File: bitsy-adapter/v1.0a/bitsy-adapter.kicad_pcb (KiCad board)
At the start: 2 copper layers, 49.5 x 36.8 mm, 17 parts, among them J1 PMOD1A, J2 PMOD1A, J3 PMOD1A, J4 5V AUX, J5 5V AUX, J6 5V AUX

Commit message: Finish bitsy-adapter v1.0a
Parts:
- removed the J5 at (160.0, 102.9)
- added J6: IO3, pkl_pin_headers:Pin_Header_Straight_Round_1x01, F.Cu at (147.3, 119.4)
- added J7: IO2, pkl_pin_headers:Pin_Header_Straight_Round_1x01, F.Cu at (149.9, 119.4)
- added LOGO1: 1BitSquared, pkl_logos:null_Logo_SilkS_4mm, B.Cu at (139.7, 130.2)
- moved A1 5.08 mm to (133.3, 114.3)
- moved R1 0.63 mm to (123.4, 103.5)
- moved R2 0.63 mm to (128.5, 103.5)
- moved R3 0.63 mm to (146.3, 103.5)
- moved R4 0.63 mm to (151.4, 103.5)
- moved R5 0.63 mm to (156.8, 109.5)
- moved R6 0.63 mm to (156.8, 114.6)
- renumbered J6 to J5
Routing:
- net GND: track 92.8 -> 101.0 mm
- net +5V: track 79.3 -> 85.0 mm
- net +3V3: track 63.2 -> 68.2 mm
- net /P2_10: track 31.1 -> 35.7 mm, vias 0 -> 1
- net /P2_8: track 18.8 -> 23.5 mm, vias 0 -> 1
- net /P2_4: track 28.3 -> 32.8 mm, vias 0 -> 1
- net /P2_2: track 16.0 -> 20.6 mm, vias 0 -> 1
- net /P2_7: track 13.3 -> 17.7 mm, vias 0 -> 1
- net /P2_9: track 25.5 -> 30.0 mm, vias 0 -> 1
- net /P2_1: track 10.5 -> 14.9 mm, vias 0 -> 1
- net /P2_3: track 22.7 -> 27.2 mm, vias 0 -> 1
- net /P1A9: track 24.1 -> 19.7 mm
- net /P1A7: track 22.0 -> 18.4 mm
- net /P1B9: track 6.07 -> 2.57 mm, vias 1 -> 0
- net /P1A8: track 22.5 -> 19.3 mm
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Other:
- board text added: ""5V" is connected to VIN on the Bitsy, which is in turn jumpered to VUSB"
- board text added: "1"
- board text added: "12"
- board text added: "3V3"
- board text added: "5V"
- board text added: "6"
- board text added: "7"
- board text added: "CC BY-SA 4.0"
- board text added: "GND"
- board text added: "IO2"
- board text added: "IO3"
- board text added: "P1A1"
- board text added: "P1A10"
- board text added: "P1A2"
- board text added: "P1A3"
- board text added: "P1A4"
- board text added: "P1A7"
- board text added: "P1A8"
- board text added: "P1A9"
- board text added: "P1B1"
- board text added: "P1B10"
- board text added: "P1B2"
- board text added: "P1B3"
- board text added: "P1B4"
- board text added: "P1B7"
- board text added: "P1B8"
- board text added: "P1B9"
- board text added: "P2_1"
- board text added: "P2_10"
- board text added: "P2_2"
- board text added: "P2_3"
- board text added: "P2_4"
- board text added: "P2_7"
- board text added: "P2_8"
- board text added: "P2_9"
- board text added: "PMOD1A"
- board text added: "PMOD1B"
- board text added: "PMOD2"
- board text added: "USB GOES HERE"
- board text added: "VIN"
- board text added: "iCEBreaker Bitsy PMOD Adapter"
- board text added: "iCEBreaker Bitsy PMOD Adapter v1.0a"
- board text added: "iCEBreaker Bitsy v1.x"
- board text added: "v1.0a"
- board text added: "© 2020 NULL"
- board text added: "© 2020 NULL CC BY-SA 4.0"
- board text removed: "iCEBreaker Bitsy"

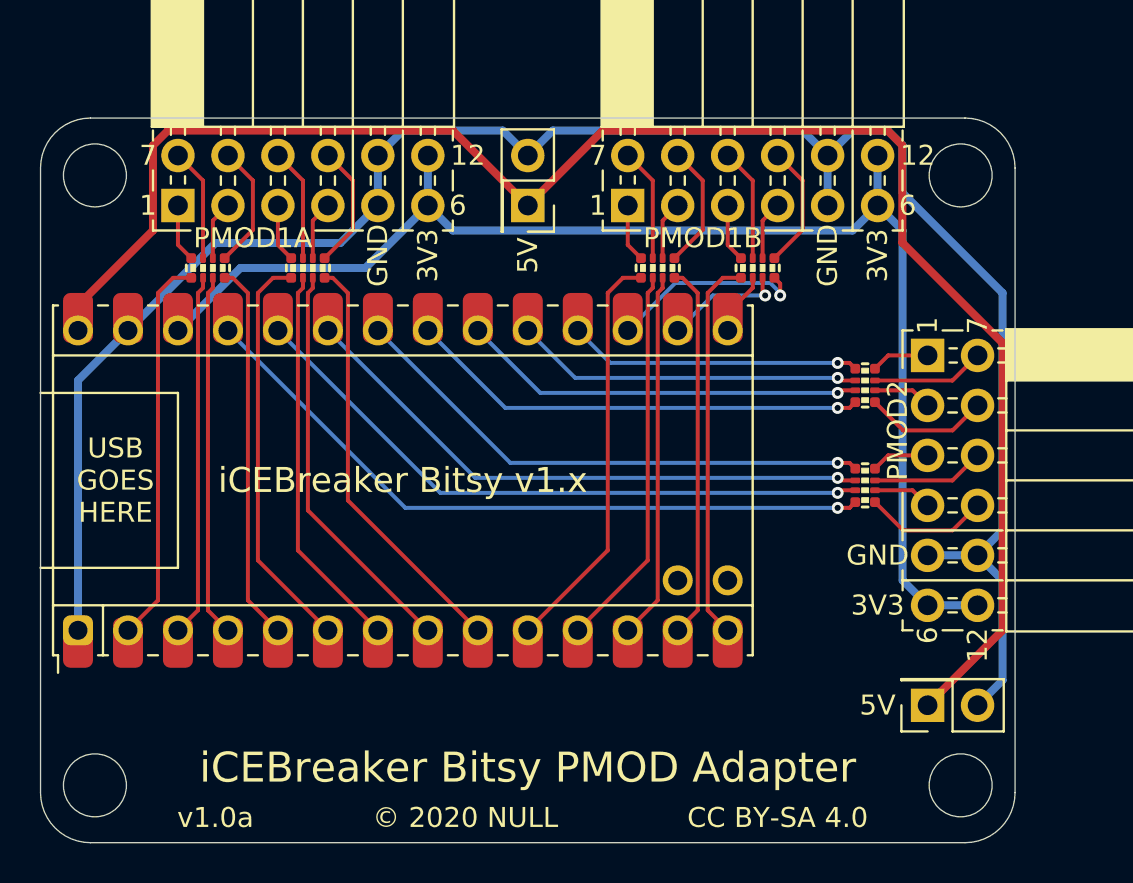
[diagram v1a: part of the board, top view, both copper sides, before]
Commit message: Change bitsy adapter pinout
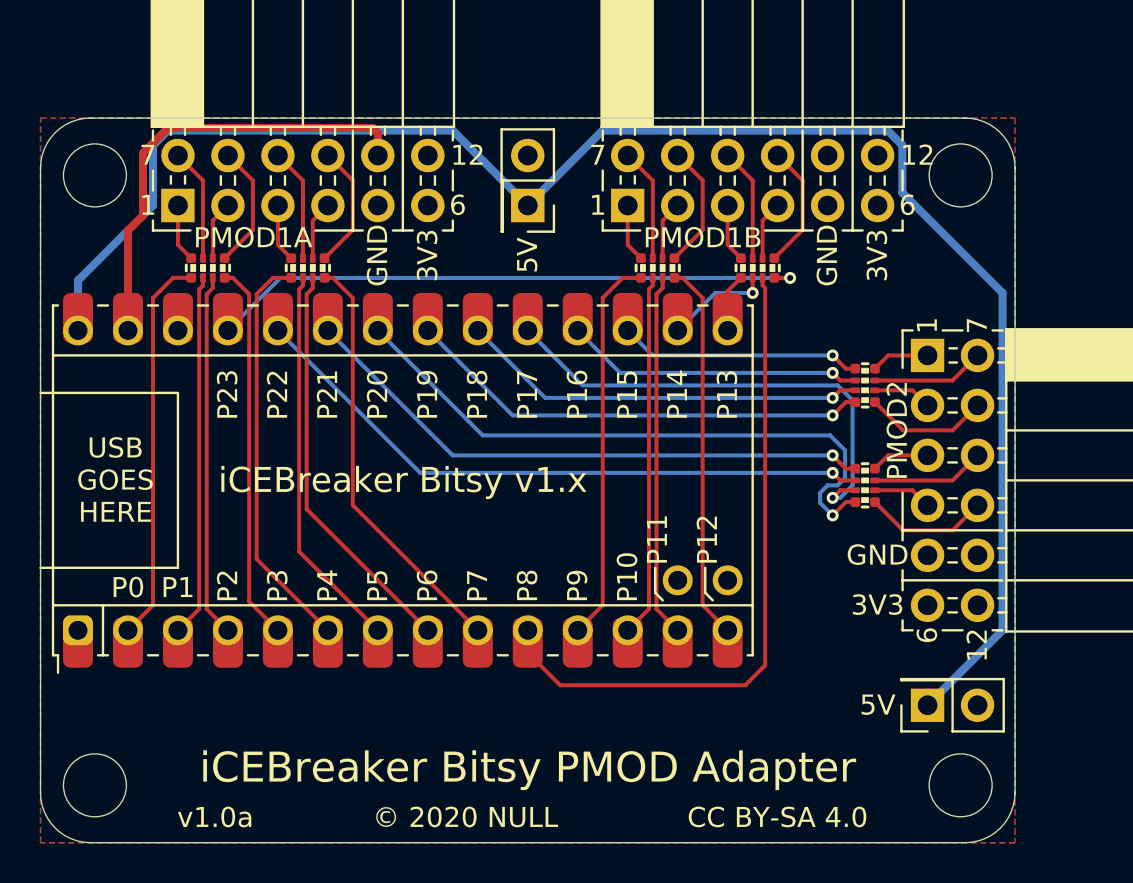
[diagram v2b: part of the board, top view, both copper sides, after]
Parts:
- J2: value PMOD1A -> PMOD1B
- J3: value PMOD1A -> PMOD2
- LOGO1: footprint pkl_logos:null_Logo_SilkS_4mm -> pkl_logos:1b2_Logo_SilkS_4mm
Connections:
- A1 pad 10: /P1B1 -> /P8
- A1 pad 11: /P1B7 -> /P9
- A1 pad 12: /P1B2 -> /P10
- A1 pad 13: /P1B8 -> /P11
- A1 pad 14: /P1B3 -> /P12
- A1 pad 15: /P1B9 -> /P13
- A1 pad 16: /P1B4 -> /P14
- A1 pad 17: /P1B10 -> /P15
- A1 pad 18: /P2_1 -> /P16
- A1 pad 19: /P2_7 -> /P17
- A1 pad 2: /P1A1 -> /P0
- A1 pad 20: /P2_2 -> /P18
- A1 pad 21: /P2_8 -> /P19
- A1 pad 22: /P2_3 -> /P20
- A1 pad 23: /P2_9 -> /P21
- A1 pad 24: /P2_4 -> /P22
- A1 pad 25: /P2_10 -> /P23
- A1 pad 3: /P1A7 -> /P1
- A1 pad 4: /P1A2 -> /P2
- A1 pad 5: /P1A8 -> /P3
- A1 pad 6: /P1A3 -> /P4
- A1 pad 7: /P1A9 -> /P5
- A1 pad 8: /P1A4 -> /P6
- A1 pad 9: /P1A10 -> /P7
- J1 pad 1: Net-(J1-Pad1) -> /P1A1
- J1 pad 10: Net-(J1-Pad10) -> /P1A10
- J1 pad 2: Net-(J1-Pad2) -> /P1A2
- J1 pad 3: Net-(J1-Pad3) -> /P1A3
- J1 pad 4: Net-(J1-Pad4) -> /P1A4
- J1 pad 7: Net-(J1-Pad7) -> /P1A7
- J1 pad 8: Net-(J1-Pad8) -> /P1A8
- J1 pad 9: Net-(J1-Pad9) -> /P1A9
- J2 pad 1: Net-(J2-Pad1) -> /P1B1
- J2 pad 10: Net-(J2-Pad10) -> /P1B10
- J2 pad 2: Net-(J2-Pad2) -> /P1B2
- J2 pad 3: Net-(J2-Pad3) -> /P1B3
- J2 pad 4: Net-(J2-Pad4) -> /P1B4
- J2 pad 7: Net-(J2-Pad7) -> /P1B7
- J2 pad 8: Net-(J2-Pad8) -> /P1B8
- J2 pad 9: Net-(J2-Pad9) -> /P1B9
- J3 pad 1: Net-(J3-Pad1) -> /P2_1
- J3 pad 10: Net-(J3-Pad10) -> /P2_10
- J3 pad 2: Net-(J3-Pad2) -> /P2_2
- J3 pad 3: Net-(J3-Pad3) -> /P2_3
- J3 pad 4: Net-(J3-Pad4) -> /P2_4
- J3 pad 7: Net-(J3-Pad7) -> /P2_7
- J3 pad 8: Net-(J3-Pad8) -> /P2_8
- J3 pad 9: Net-(J3-Pad9) -> /P2_9
- R1 pad 1: /P1A1 -> /P0
- R1 pad 2: Net-(J1-Pad1) -> /P1A1
- R1 pad 3: /P1A7 -> /P1
- R1 pad 4: Net-(J1-Pad7) -> /P1A7
- R1 pad 5: /P1A2 -> /P2
- R1 pad 6: Net-(J1-Pad2) -> /P1A2
- R1 pad 7: /P1A8 -> /P3
- R1 pad 8: Net-(J1-Pad8) -> /P1A8
- R2 pad 1: /P1A3 -> /P4
- R2 pad 2: Net-(J1-Pad3) -> /P1A3
- R2 pad 3: /P1A9 -> /P5
- R2 pad 4: Net-(J1-Pad9) -> /P1A9
- R2 pad 5: /P1A4 -> /P6
- R2 pad 6: Net-(J1-Pad4) -> /P1A4
- R2 pad 7: /P1A10 -> /P7
- R2 pad 8: Net-(J1-Pad10) -> /P1A10
- R3 pad 1: /P1B1 -> /P9
- R3 pad 2: Net-(J2-Pad1) -> /P1B1
- R3 pad 3: /P1B7 -> /P10
- R3 pad 4: Net-(J2-Pad7) -> /P1B7
- R3 pad 5: /P1B2 -> /P11
- R3 pad 6: Net-(J2-Pad2) -> /P1B2
- R3 pad 7: /P1B8 -> /P12
- R3 pad 8: Net-(J2-Pad8) -> /P1B8
- R4 pad 1: /P1B3 -> /P13
- R4 pad 2: Net-(J2-Pad3) -> /P1B3
- R4 pad 3: /P1B9 -> /P14
- R4 pad 4: Net-(J2-Pad9) -> /P1B9
- R4 pad 5: /P1B4 -> /P8
- R4 pad 6: Net-(J2-Pad4) -> /P1B4
- R4 pad 7: /P1B10 -> /P23
- R4 pad 8: Net-(J2-Pad10) -> /P1B10
- R5 pad 1: /P2_1 -> /P15
- R5 pad 2: Net-(J3-Pad1) -> /P2_1
- R5 pad 3: /P2_7 -> /P16
- R5 pad 4: Net-(J3-Pad7) -> /P2_7
- R5 pad 5: /P2_2 -> /P18
- R5 pad 6: Net-(J3-Pad2) -> /P2_2
- R5 pad 7: /P2_8 -> /P19
- R5 pad 8: Net-(J3-Pad8) -> /P2_8
- R6 pad 1: /P2_3 -> /P21
- R6 pad 2: Net-(J3-Pad3) -> /P2_3
- R6 pad 3: /P2_9 -> /P22
- R6 pad 4: Net-(J3-Pad9) -> /P2_9
- R6 pad 5: /P2_4 -> /P17
- R6 pad 6: Net-(J3-Pad4) -> /P2_4
- R6 pad 7: /P2_10 -> /P20
- R6 pad 8: Net-(J3-Pad10) -> /P2_10
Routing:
- net GND: track 101.0 -> 22.4 mm
- net +3V3: track 68.2 -> 0.00 mm
- net /P8: track 0.00 -> 33.4 mm
- net /P22: track 0.00 -> 32.5 mm, vias 0 -> 1
- net /P20: track 0.00 -> 32.1 mm, vias 0 -> 1
- net /P23: track 0.00 -> 30.5 mm, vias 0 -> 1
- net /P2_4: track 32.8 -> 2.99 mm, vias 1 -> 0
- net /P21: track 0.00 -> 29.7 mm, vias 0 -> 1
- net /P2_10: track 35.7 -> 6.34 mm, vias 1 -> 0
- net /P17: track 0.00 -> 24.9 mm, vias 0 -> 1
- net /P2_9: track 30.0 -> 5.74 mm, vias 1 -> 0
- net /P2_3: track 27.2 -> 2.95 mm, vias 1 -> 0
- net /P19: track 0.00 -> 23.8 mm, vias 0 -> 1
- net /P7: track 0.00 -> 21.4 mm
- net /P18: track 0.00 -> 20.8 mm, vias 0 -> 1
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- added copper zone on B.Cu, net +3V3
- added copper zone on F.Cu, net GND
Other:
- board text added: "P0"
- board text added: "P1"
- board text added: "P10"
- board text added: "P11"
- board text added: "P12"
- board text added: "P13"
- board text added: "P14"
- board text added: "P15"
- board text added: "P16"
- board text added: "P17"
- board text added: "P18"
- board text added: "P19"
- board text added: "P2"
- board text added: "P20"
- board text added: "P21"
- board text added: "P22"
- board text added: "P23"
- board text added: "P3"
- board text added: "P4"
- board text added: "P5"
- board text added: "P6"
- board text added: "P7"
- board text added: "P8"
- board text added: "P9"

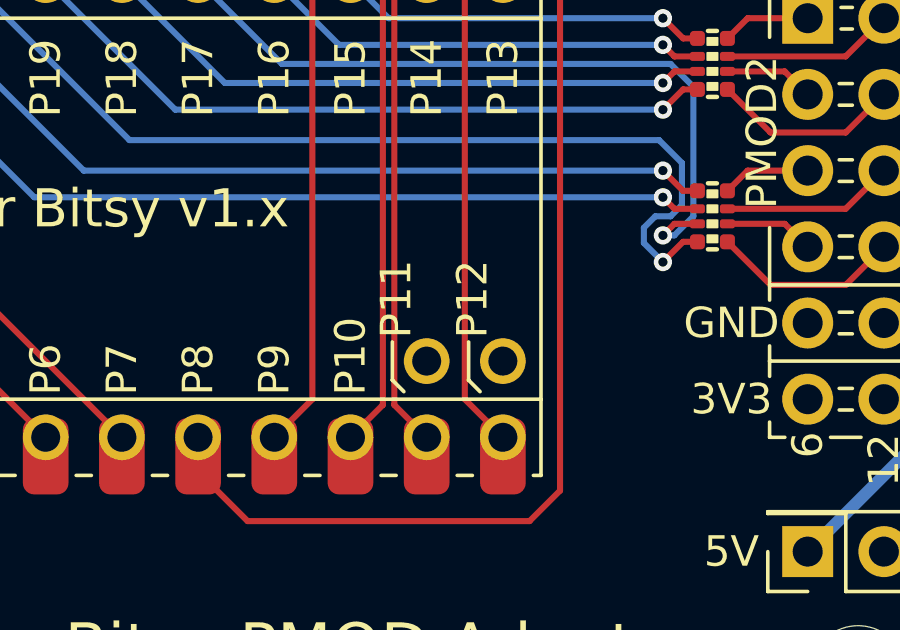
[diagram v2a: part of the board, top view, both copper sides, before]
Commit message: Bitsy Adapter: Remove unused IO2 & IO3 pins
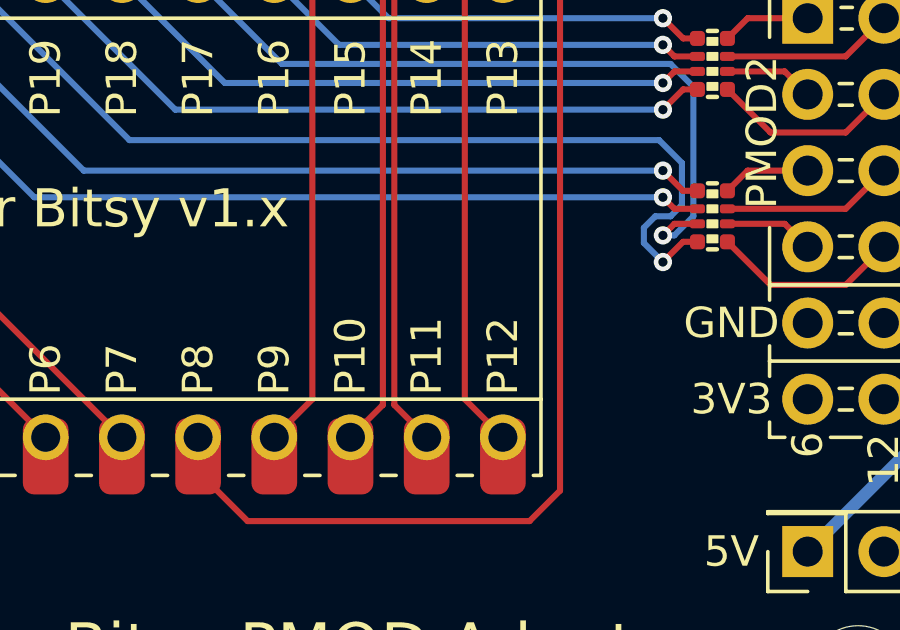
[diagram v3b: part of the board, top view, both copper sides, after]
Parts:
- removed J6: IO3, pkl_pin_headers:Pin_Header_Straight_Round_1x01
- removed J7: IO2, pkl_pin_headers:Pin_Header_Straight_Round_1x01
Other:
- board text added: "5V is connected to VIN on the Bitsy, which is in turn jumpered to VUSB"
- board text removed: ""5V" is connected to VIN on the Bitsy, which is in turn jumpered to VUSB"
- board text removed: "IO2"
- board text removed: "IO3"

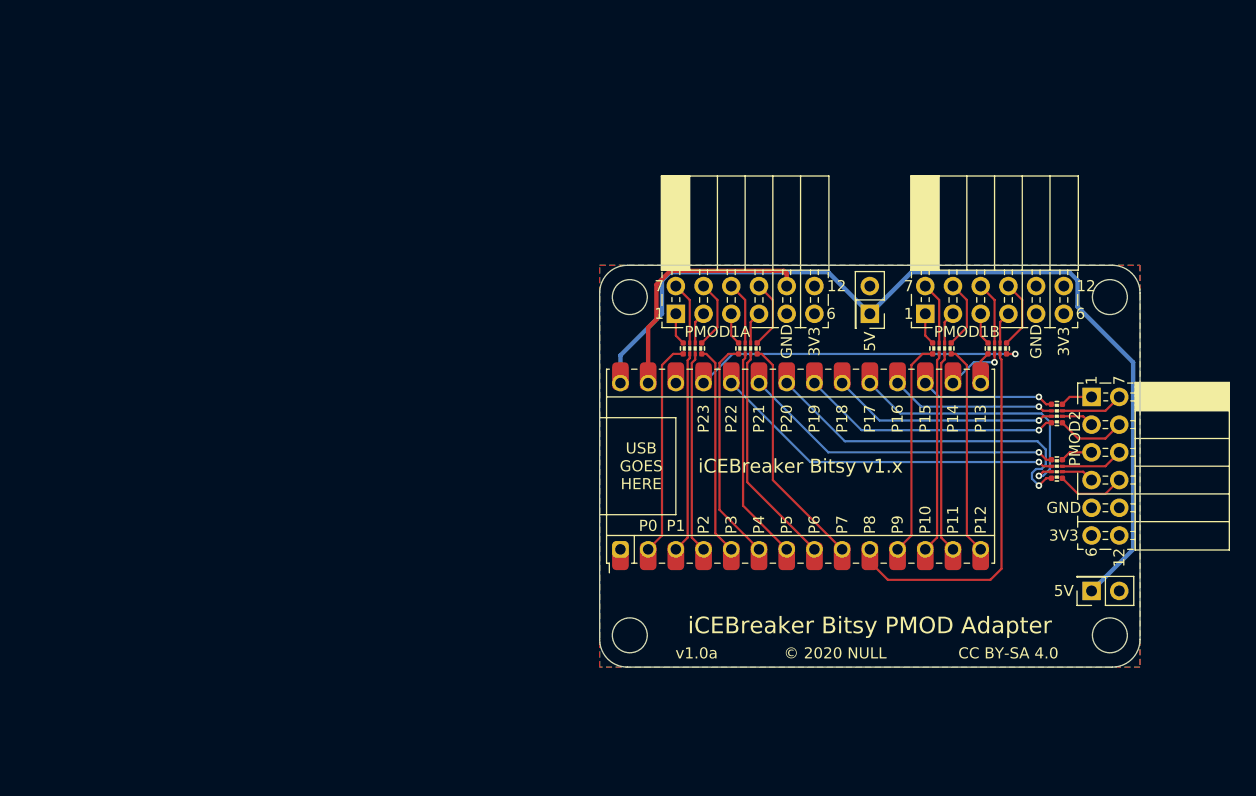
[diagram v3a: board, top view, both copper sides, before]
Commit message: Bitsy Adapter: Completely change pinout/formfactor
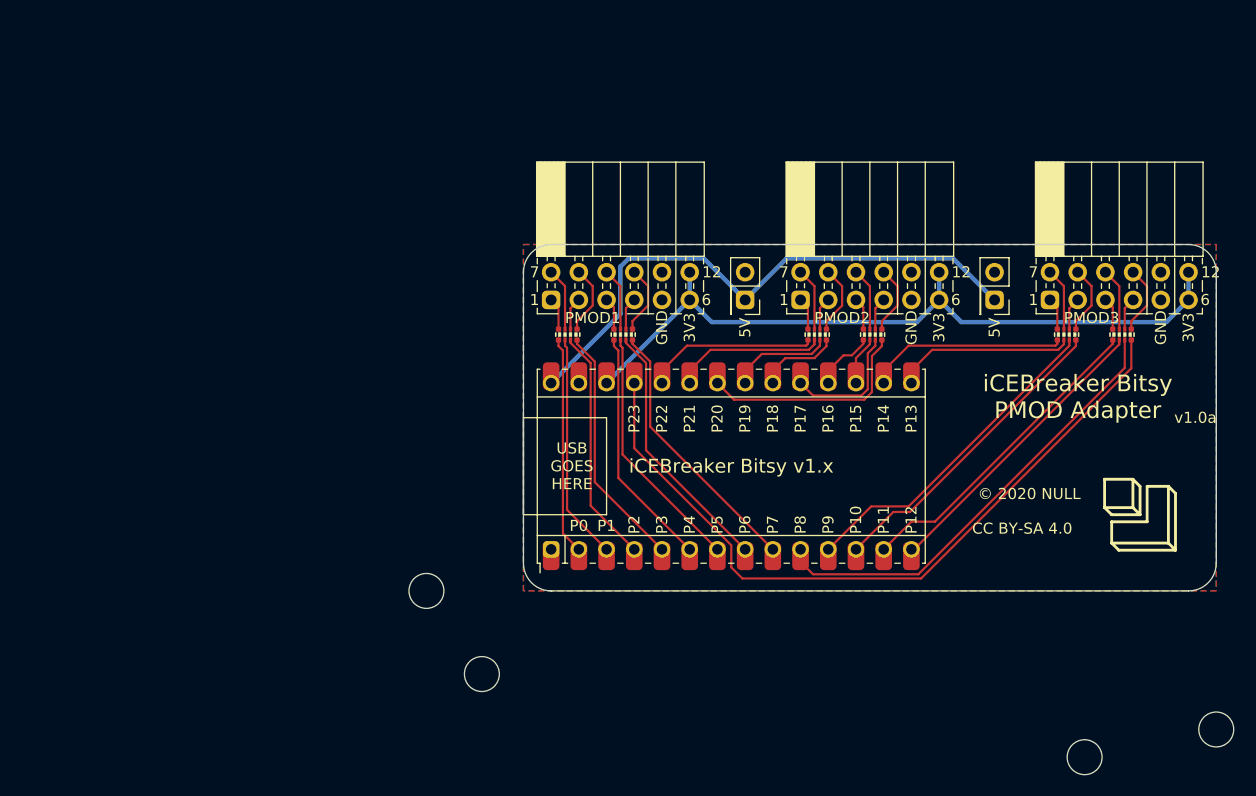
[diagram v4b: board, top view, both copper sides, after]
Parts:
- J1: value PMOD1A -> PMOD1
- J2: value PMOD1B -> PMOD2
- J3: value PMOD2 -> PMOD3
- LOGO1: footprint pkl_logos:1b2_Logo_SilkS_4mm -> pkl_logos:1b2_Logo_SilkS_6.5mm; moved to F.Cu
- moved H2 42.2 mm to (159.4, 141.0)
- moved H1 32.8 mm to (99.1, 125.7)
- moved J5 28.1 mm to (151.1, 99.1), turned to 270 degrees
- moved LOGO1 27.3 mm to (164.5, 118.7), turned to 0 degrees
- moved H4 14.0 mm to (104.1, 133.3)
- moved R6 13.7 mm to (162.8, 102.2), turned to 90 degrees
- moved H3 13.0 mm to (171.4, 138.4)
- moved J1 11.5 mm to (110.5, 99.1)
- moved J2 11.5 mm to (133.3, 99.1)
- moved R1 11.5 mm to (112.0, 102.2)
- moved R2 11.5 mm to (117.1, 102.2)
- moved R3 11.5 mm to (134.9, 102.2)
- moved J4 11.5 mm to (128.3, 99.1)
- moved R4 11.5 mm to (140.0, 102.2)
- moved J3 9.67 mm to (156.2, 99.1), turned to 90 degrees
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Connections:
- net /P1A1 renamed /J1P1
- net /P1A10 renamed /J1P10
- net /P1A2 renamed /J1P2
- net /P1A3 renamed /J1P3
- net /P1A4 renamed /J1P4
- net /P1A7 renamed /J1P7
- net /P1A8 renamed /J1P8
- net /P1A9 renamed /J1P9
- net /P1B1 renamed /J2P1
- net /P1B10 renamed /J2P10
- net /P1B2 renamed /J2P2
- net /P1B3 renamed /J2P3
- net /P1B4 renamed /J2P4
- net /P1B7 renamed /J2P7
- net /P1B8 renamed /J2P8
- net /P1B9 renamed /J2P9
- net /P2_1 renamed /J3P1
- net /P2_10 renamed /J3P10
- net /P2_2 renamed /J3P2
- net /P2_3 renamed /J3P3
- net /P2_4 renamed /J3P4
- net /P2_7 renamed /J3P7
- net /P2_8 renamed /J3P8
- net /P2_9 renamed /J3P9
- R3 pad 1: /P9 -> /P22
- R3 pad 3: /P10 -> /P21
- R3 pad 5: /P11 -> /P19
- R3 pad 7: /P12 -> /P18
- R4 pad 1: /P13 -> /P16
- R4 pad 3: /P14 -> /P15
- R4 pad 5: /P8 -> /P17
- R4 pad 7: /P23 -> /P20
- R5 pad 1: /P15 -> /P14
- R5 pad 3: /P16 -> /P13
- R5 pad 5: /P18 -> /P9
- R5 pad 7: /P19 -> /P10
- R6 pad 1: /P21 -> /P11
- R6 pad 3: /P22 -> /P12
- R6 pad 5: /P17 -> /P8
- R6 pad 7: /P20 -> /P23
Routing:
- net +3V3: track 0.00 -> 67.5 mm
- net /P23: track 30.5 -> 68.2 mm, vias 1 -> 0
- net +5V: track 85.0 -> 52.6 mm
- net GND: track 22.4 -> 0.00 mm
- net /P22: track 32.5 -> 15.2 mm, vias 1 -> 0
- net /P21: track 29.7 -> 13.3 mm, vias 1 -> 0
- net /P19: track 23.8 -> 8.83 mm, vias 1 -> 0
- net /P18: track 20.8 -> 6.91 mm, vias 1 -> 0
- net /P13: track 2.37 -> 15.9 mm
- net /P17: track 24.9 -> 11.7 mm, vias 1 -> 0
- net /P14: track 5.37 -> 17.8 mm, vias 1 -> 0
- net /P20: track 32.1 -> 20.2 mm, vias 1 -> 0
- net /P11: track 18.5 -> 29.1 mm
- net /P9: track 19.8 -> 30.3 mm
- net /P16: track 15.2 -> 5.09 mm, vias 1 -> 0
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- added copper zone on B.Cu, net GND
- removed copper zone on B.Cu, net +3V3
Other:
- board size 49.5 x 36.8 mm -> 63.5 x 31.8 mm
- board text added: "PMOD1"
- board text added: "PMOD3"
